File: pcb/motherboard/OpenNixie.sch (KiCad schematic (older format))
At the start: 137 parts, among them J1 Conn_01x02, J10 Conn_01x10, J2 Conn_01x03, J3 Conn_01x03, J4 DC 12V, J5 Conn_01x04, J6 Conn_01x03, J7 Conn_01x10, J8 Conn_01x10, J9 Conn_01x10, Q1 S8050, Q10 MPSA42, Q11 MPSA42, Q12 MPSA42, Q13 MPSA42, Q14 MPSA42, Q15 MPSA42, Q16 MPSA42, Q17 MPSA42, Q18 MPSA42, Q19 MPSA42, Q2 IRFB4620, Q20 MPSA42, Q21 MPSA42, Q22 MPSA42, Q23 MPSA42, Q24 MPSA42, Q25 MPSA42, Q26 MPSA42, Q27 MPSA42, Q28 MPSA42, Q29 MPSA42, Q3 MPSA42, Q30 MPSA42, Q31 MPSA42, Q32 MPSA42, Q33 MPSA42, Q34 MPSA42, Q35 MPSA42, Q36 MPSA42, Q37 MPSA42, Q38 MPSA42, Q39 MPSA42, Q4 MPSA42, Q40 MPSA42, Q41 MPSA42, Q42 MPSA42, Q5 MPSA42, Q6 MPSA42, Q7 MPSA42, Q8 MPSA42, Q9 MPSA42, SW1 SW_SPST, U1 LM7805_TO220, U10 74LS138, U11 74LS138, U12 74LS138, U13 74LS138, U14 74HC595, U15 74LS138, U16 74LS138, U2 NE555P, U3 MAX1771CSA, U4 DS3231M, U5 24LC16, U6 TSDP341xx, U7 74LS138, U8 74LS138, U9 74HC595

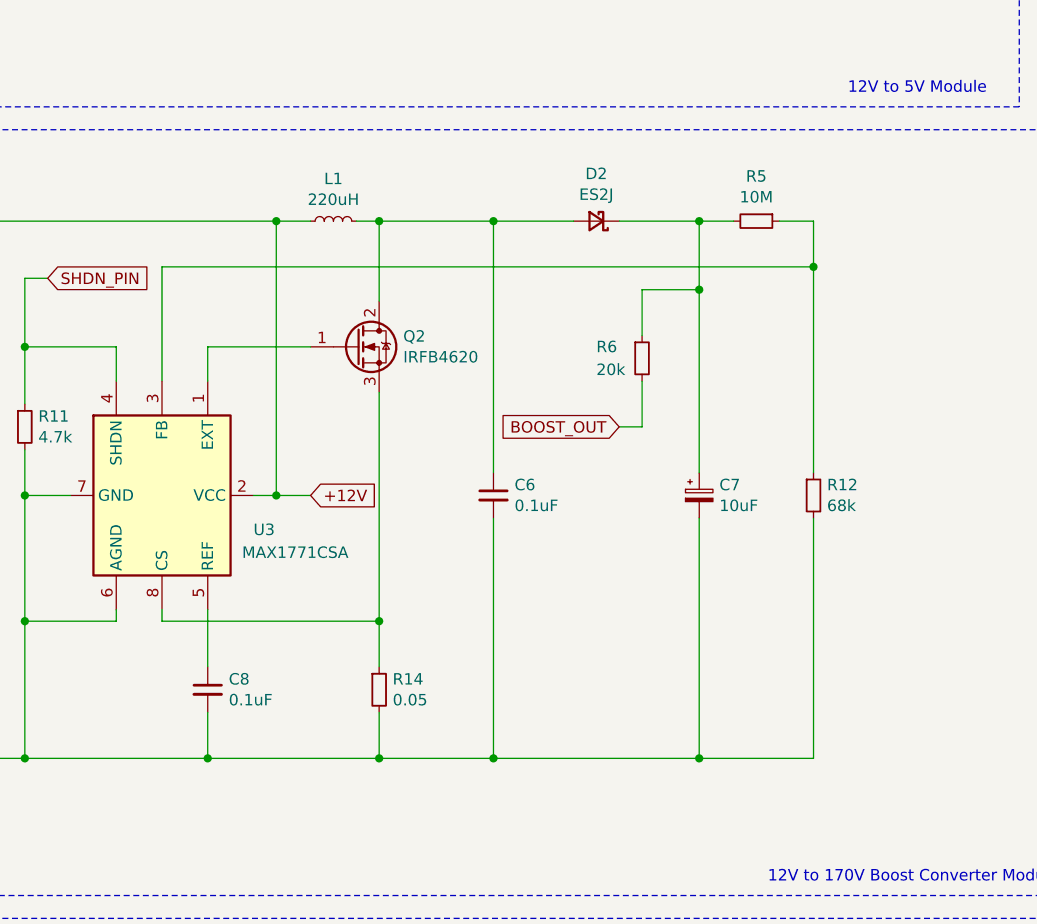
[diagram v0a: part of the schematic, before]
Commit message: Fix layout errors
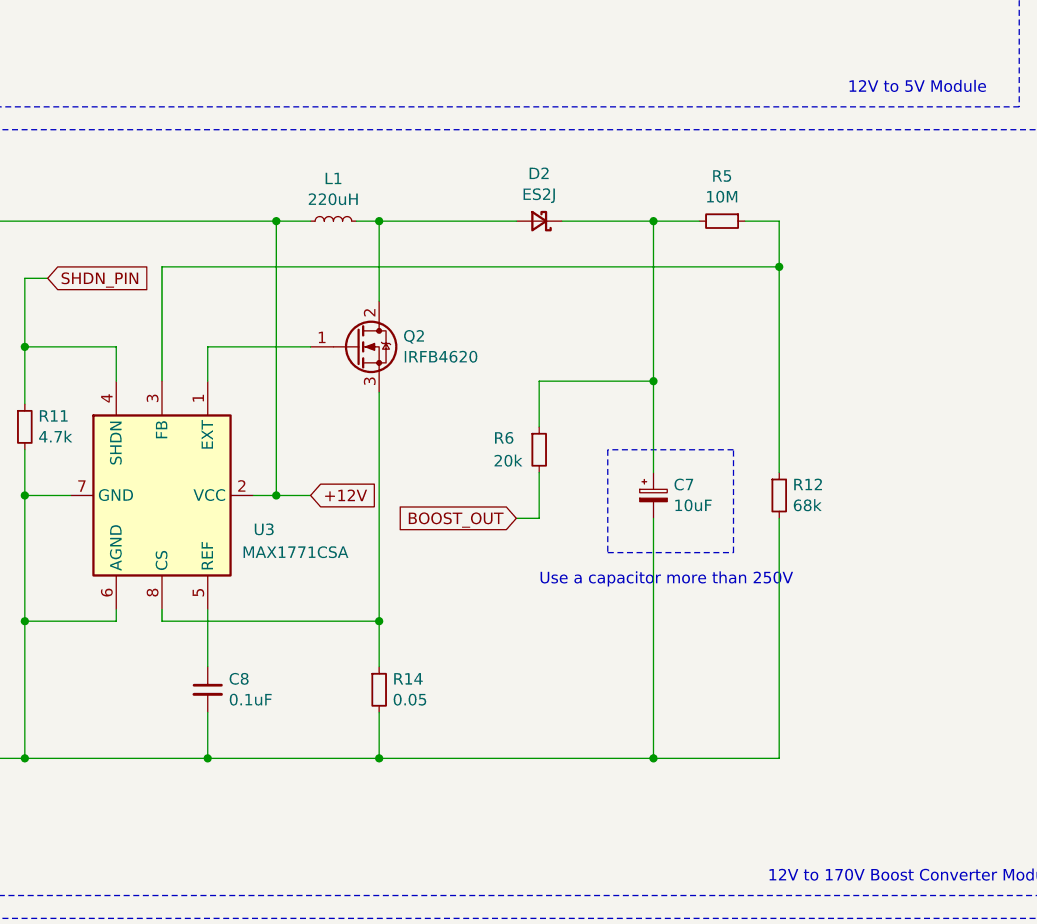
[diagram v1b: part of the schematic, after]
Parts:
- removed C6: 0.1uF, Capacitor_THT:C_Disc_D3.0mm_W2.0mm_P2.50mm, symbol Device:C_Small
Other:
- note added: "Use a capacitor more than 250V"
- moved on the sheet: C7, D2, R12, R5, R6
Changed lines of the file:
@@
 Connection ~ 9500 2450
 Wire Wire Line
-	4950 6100 5450 6100
-Connection ~ 4950 6100
+	4250 4450 4750 4450
 Wire Wire Line
-	4700 4050 4950 4050
-Wire Wire Line
-	2600 3950 5450 3950
-Wire Wire Line
-	4050 6100 4950 6100
-Text GLabel 4600 4650 0    50   Input ~ 0
+	2600 3950 5300 3950
+Text GLabel 4150 5050 0    50   Input ~ 0
 BOOST_OUT
 Wire Wire Line
@@
 Text GLabel 2100 4000 2    50   Input ~ 0
 SHDN_PIN
-Connection ~ 5450 3950
+Connection ~ 5300 3950
 Wire Wire Line
-	5450 3950 5450 4850
+	5300 3950 5300 4850
 Connection ~ 3100 4950
 Wire Wire Line
@@
 	2600 5450 2600 5500
 Wire Wire Line
-	3550 6100 4050 6100
-Connection ~ 4050 6100
-Wire Wire Line
-	4950 5050 4950 6100
+	4750 5050 4750 6100
 $Comp
 L Device:CP_Small C7
 U 1 1 63E82EE3
-P 4950 4950
-F 0 "C7" H 5038 4996 50  0000 L CNN
-F 1 "10uF" H 5038 4905 50  0000 L CNN
-F 2 "Capacitor_THT:CP_Radial_D5.0mm_P2.50mm" H 4950 4950 50  0001 C CNN
-F 3 "~" H 4950 4950 50  0001 C CNN
-	1    4950 4950
+P 4750 4950
+F 0 "C7" H 4838 4996 50  0000 L CNN
+F 1 "10uF" H 4838 4905 50  0000 L CNN
+F 2 "Capacitor_THT:CP_Radial_D5.0mm_P2.50mm" H 4750 4950 50  0001 C CNN
+F 3 "~" H 4750 4950 50  0001 C CNN
+	1    4750 4950
 	1    0    0    -1
 $EndComp
 Wire Wire Line
-	5450 5050 5450 6100
+	5300 5050 5300 6100
 $Comp
 L Device:R_Small R12
 U 1 1 63E66239
-P 5450 4950
-F 0 "R12" H 5509 4996 50  0000 L CNN
-F 1 "68k" H 5509 4905 50  0000 L CNN
-F 2 "Resistor_THT:R_Axial_DIN0204_L3.6mm_D1.6mm_P7.62mm_Horizontal" H 5450 4950 50  0001 C CNN
-F 3 "~" H 5450 4950 50  0001 C CNN
-	1    5450 4950
+P 5300 4950
+F 0 "R12" H 5359 4996 50  0000 L CNN
+F 1 "68k" H 5359 4905 50  0000 L CNN
+F 2 "Resistor_THT:R_Axial_DIN0204_L3.6mm_D1.6mm_P7.62mm_Horizontal" H 5300 4950 50  0001 C CNN
+F 3 "~" H 5300 4950 50  0001 C CNN
+	1    5300 4950
 	1    0    0    -1
 $EndComp
@@
 	1    0    0    -1
 $EndComp
-Wire Wire Line
-	4050 5050 4050 6100
-$Comp
-L Device:C_Small C6
-U 1 1 63DAEE6F
-P 4050 4950
-F 0 "C6" H 4142 4996 50  0000 L CNN
-F 1 "0.1uF" H 4142 4905 50  0000 L CNN
-F 2 "Capacitor_THT:C_Disc_D3.0mm_W2.0mm_P2.50mm" H 4050 4950 50  0001 C CNN
-F 3 "~" H 4050 4950 50  0001 C CNN
-	1    4050 4950
-	1    0    0    -1
-$EndComp
 Connection ~ 2800 6100
 Wire Wire Line
@@
 $EndComp
 Wire Wire Line
-	4600 4650 4700 4650
-Connection ~ 4950 4050
-Wire Wire Line
-	4950 4050 4950 4850
+	4150 5050 4250 5050
 Wire Wire Line
-	4700 4050 4700 4250
+	4250 4450 4250 4650
 Wire Wire Line
-	4700 4450 4700 4650
+	4250 4850 4250 5050
 $Comp
 L Device:R_Small R6
 U 1 1 6A87AE72
-P 4700 4350
-F 0 "R6" H 4500 4400 50  0000 L CNN
-F 1 "20k" H 4500 4300 50  0000 L CNN
-F 2 "Resistor_THT:R_Axial_DIN0204_L3.6mm_D1.6mm_P7.62mm_Horizontal" H 4700 4350 50  0001 C CNN
-F 3 "~" H 4700 4350 50  0001 C CNN
-	1    4700 4350
+P 4250 4750
+F 0 "R6" H 4050 4800 50  0000 L CNN
+F 1 "20k" H 4050 4700 50  0000 L CNN
+F 2 "Resistor_THT:R_Axial_DIN0204_L3.6mm_D1.6mm_P7.62mm_Horizontal" H 4250 4750 50  0001 C CNN
+F 3 "~" H 4250 4750 50  0001 C CNN
+	1    4250 4750
 	1    0    0    -1
 $EndComp
@@
 	1    0    0    -1
 $EndComp
-Wire Wire Line
-	4950 4050 4950 3750
 $Comp
 L Device:L_Small L1
@@
 $EndComp
 Wire Wire Line
-	4050 3750 4050 4850
-Wire Wire Line
 	1500 4850 1500 3750
 $Comp
 L Device:D_Schottky_Small D2
 U 1 1 63E25C25
-P 4500 3750
-F 0 "D2" H 4500 3543 50  0000 C CNN
-F 1 "ES2J" H 4500 3634 50  0000 C CNN
-F 2 "Diode_SMD:D_SMA" V 4500 3750 50  0001 C CNN
-F 3 "~" V 4500 3750 50  0001 C CNN
-	1    4500 3750
+P 4250 3750
+F 0 "D2" H 4250 3543 50  0000 C CNN
+F 1 "ES2J" H 4250 3634 50  0000 C CNN
+F 2 "Diode_SMD:D_SMA" V 4250 3750 50  0001 C CNN
+F 3 "~" V 4250 3750 50  0001 C CNN
+	1    4250 3750
 	-1   0    0    1
 $EndComp
 Wire Wire Line
-	4600 3750 4950 3750
+	4350 3750 4750 3750
 $Comp
 L Device:R_Small R5
 U 1 1 63E5A426
-P 5200 3750
-F 0 "R5" V 5004 3750 50  0000 C CNN
-F 1 "10M" V 5095 3750 50  0000 C CNN
-F 2 "Resistor_THT:R_Axial_DIN0204_L3.6mm_D1.6mm_P7.62mm_Horizontal" H 5200 3750 50  0001 C CNN
-F 3 "~" H 5200 3750 50  0001 C CNN
-	1    5200 3750
+P 5050 3750
+F 0 "R5" V 4854 3750 50  0000 C CNN
+F 1 "10M" V 4945 3750 50  0000 C CNN
+F 2 "Resistor_THT:R_Axial_DIN0204_L3.6mm_D1.6mm_P7.62mm_Horizontal" H 5050 3750 50  0001 C CNN
+F 3 "~" H 5050 3750 50  0001 C CNN
+	1    5050 3750
 	0    1    1    0
 $EndComp
 Wire Wire Line
-	5300 3750 5450 3750
-Connection ~ 4050 3750
-Wire Wire Line
-	4050 3750 4400 3750
+	5150 3750 5300 3750
 Wire Wire Line
 	1500 3750 3100 3750
@@
 	3100 3750 3100 4950
 Wire Wire Line
-	3550 3750 4050 3750
-Wire Wire Line
 	3450 3750 3550 3750
 Connection ~ 3550 3750
@@
 	3550 3750 3550 4100
 Wire Wire Line
-	5450 3750 5450 3950
-Connection ~ 4950 3750
-Wire Wire Line
-	4950 3750 5100 3750
+	5300 3750 5300 3950
 Wire Notes Line
 	15300 3250 22800 3250
@@
 	1    0    0    -1
 $EndComp
+Wire Wire Line
+	3550 6100 4750 6100
+Wire Wire Line
+	3550 3750 4150 3750
+Connection ~ 4750 4450
+Wire Wire Line
+	4750 4450 4750 4850
+Wire Wire Line
+	4750 3750 4750 4450
+Connection ~ 4750 3750
+Connection ~ 4750 6100
+Wire Wire Line
+	4750 6100 5300 6100
+Wire Wire Line
+	4750 3750 4950 3750
+Wire Notes Line
+	4550 4750 4550 5200
+Wire Notes Line
+	4550 5200 5100 5200
+Wire Notes Line
+	5100 5200 5100 4750
+Wire Notes Line
+	5100 4750 4550 4750
+Text Notes 4250 5350 0    50   ~ 0
+Use a capacitor more than 250V
 Wire Bus Line
 	11050 13150 11050 14500

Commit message: Change footprint
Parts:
- C7: footprint Capacitor_THT:CP_Radial_D5.0mm_P2.50mm -> Capacitor_THT:CP_Radial_D8.0mm_P3.80mm
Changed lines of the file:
@@
 F 0 "C7" H 4838 4996 50  0000 L CNN
 F 1 "10uF" H 4838 4905 50  0000 L CNN
-F 2 "Capacitor_THT:CP_Radial_D5.0mm_P2.50mm" H 4750 4950 50  0001 C CNN
+F 2 "Capacitor_THT:CP_Radial_D8.0mm_P3.80mm" H 4750 4950 50  0001 C CNN
 F 3 "~" H 4750 4950 50  0001 C CNN
 	1    4750 4950

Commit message: Fixes
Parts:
- removed Q2: IRFB4620, Package_TO_SOT_THT:TO-220-3_Horizontal_TabDown, symbol Nixie_Clock:IRFB4620
- added Q2: TK8P65W, Package_TO_SOT_SMD:TO-252-2, symbol Nixie_Clock:TK8P65W
- R6: value 20k -> 47k
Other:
- moved on the sheet: D2
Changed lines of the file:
@@
 Wire Wire Line
 	5300 5050 5300 6100
-$Comp
-L Device:R_Small R12
-U 1 1 63E66239
-P 5300 4950
-F 0 "R12" H 5359 4996 50  0000 L CNN
-F 1 "68k" H 5359 4905 50  0000 L CNN
-F 2 "Resistor_THT:R_Axial_DIN0204_L3.6mm_D1.6mm_P7.62mm_Horizontal" H 5300 4950 50  0001 C CNN
-F 3 "~" H 5300 4950 50  0001 C CNN
-	1    5300 4950
-	1    0    0    -1
-$EndComp
 Wire Wire Line
 	2000 4300 2400 4300
@@
 	4250 4850 4250 5050
 $Comp
-L Device:R_Small R6
-U 1 1 6A87AE72
-P 4250 4750
-F 0 "R6" H 4050 4800 50  0000 L CNN
-F 1 "20k" H 4050 4700 50  0000 L CNN
-F 2 "Resistor_THT:R_Axial_DIN0204_L3.6mm_D1.6mm_P7.62mm_Horizontal" H 4250 4750 50  0001 C CNN
-F 3 "~" H 4250 4750 50  0001 C CNN
-	1    4250 4750
-	1    0    0    -1
-$EndComp
-$Comp
 L Nixie_Clock:MAX1771CSA U3
 U 1 1 63E16B68
@@
 	2800 4300 3250 4300
 $Comp
-L Nixie_Clock:IRFB4620 Q2
-U 1 1 63FF12BB
-P 3450 4300
-F 0 "Q2" H 3655 4346 50  0000 L CNN
-F 1 "IRFB4620" H 3655 4255 50  0000 L CNN
-F 2 "Package_TO_SOT_THT:TO-220-3_Horizontal_TabDown" H 3450 4300 50  0001 C CIN
-F 3 "" H 3450 4300 50  0001 L CNN
-	1    3450 4300
-	1    0    0    -1
-$EndComp
-$Comp
 L Device:L_Small L1
 U 1 1 63D8F31B
@@
 L Device:D_Schottky_Small D2
 U 1 1 63E25C25
-P 4250 3750
-F 0 "D2" H 4250 3543 50  0000 C CNN
-F 1 "ES2J" H 4250 3634 50  0000 C CNN
-F 2 "Diode_SMD:D_SMA" V 4250 3750 50  0001 C CNN
-F 3 "~" V 4250 3750 50  0001 C CNN
-	1    4250 3750
+P 4150 3750
+F 0 "D2" H 4150 3543 50  0000 C CNN
+F 1 "ES2J" H 4150 3634 50  0000 C CNN
+F 2 "Diode_SMD:D_SMA" V 4150 3750 50  0001 C CNN
+F 3 "~" V 4150 3750 50  0001 C CNN
+	1    4150 3750
 	-1   0    0    1
 $EndComp
 Wire Wire Line
-	4350 3750 4750 3750
-$Comp
-L Device:R_Small R5
-U 1 1 63E5A426
-P 5050 3750
-F 0 "R5" V 4854 3750 50  0000 C CNN
-F 1 "10M" V 4945 3750 50  0000 C CNN
-F 2 "Resistor_THT:R_Axial_DIN0204_L3.6mm_D1.6mm_P7.62mm_Horizontal" H 5050 3750 50  0001 C CNN
-F 3 "~" H 5050 3750 50  0001 C CNN
-	1    5050 3750
-	0    1    1    0
-$EndComp
+	4250 3750 4750 3750
 Wire Wire Line
 	5150 3750 5300 3750
@@
 	3550 6100 4750 6100
 Wire Wire Line
-	3550 3750 4150 3750
+	3550 3750 4050 3750
 Connection ~ 4750 4450
 Wire Wire Line
@@
 Wire Notes Line
 	5100 4750 4550 4750
+$Comp
+L Nixie_Clock:TK8P65W Q2
+U 1 1 641075BE
+P 3450 4300
+F 0 "Q2" H 3654 4346 50  0000 L CNN
+F 1 "TK8P65W" H 3654 4255 50  0000 L CNN
+F 2 "Package_TO_SOT_SMD:TO-252-2" H 3450 4300 50  0001 C CIN
+F 3 "" H 3450 4300 50  0001 L CNN
+	1    3450 4300
+	1    0    0    -1
+$EndComp
+$Comp
+L Device:R_Small R12
+U 1 1 63E66239
+P 5300 4950
+F 0 "R12" H 5359 4996 50  0000 L CNN
+F 1 "68k" H 5359 4905 50  0000 L CNN
+F 2 "Resistor_THT:R_Axial_DIN0204_L3.6mm_D1.6mm_P7.62mm_Horizontal" H 5300 4950 50  0001 C CNN
+F 3 "~" H 5300 4950 50  0001 C CNN
+	1    5300 4950
+	1    0    0    -1
+$EndComp
+$Comp
+L Device:R_Small R5
+U 1 1 63E5A426
+P 5050 3750
+F 0 "R5" V 4854 3750 50  0000 C CNN
+F 1 "10M" V 4945 3750 50  0000 C CNN
+F 2 "Resistor_THT:R_Axial_DIN0204_L3.6mm_D1.6mm_P7.62mm_Horizontal" H 5050 3750 50  0001 C CNN
+F 3 "~" H 5050 3750 50  0001 C CNN
+	1    5050 3750
+	0    1    1    0
+$EndComp
 Text Notes 4250 5350 0    50   ~ 0
 Use a capacitor more than 250V
+$Comp
+L Device:R_Small R6
+U 1 1 6A87AE72
+P 4250 4750
+F 0 "R6" H 4050 4800 50  0000 L CNN
+F 1 "47k" H 4050 4700 50  0000 L CNN
+F 2 "Resistor_THT:R_Axial_DIN0204_L3.6mm_D1.6mm_P7.62mm_Horizontal" H 4250 4750 50  0001 C CNN
+F 3 "~" H 4250 4750 50  0001 C CNN
+	1    4250 4750
+	1    0    0    -1
+$EndComp
 Wire Bus Line
 	11050 13150 11050 14500

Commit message: Updates on resistor values
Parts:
- R6: value 47k -> 20k
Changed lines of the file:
@@
 P 4250 4750
 F 0 "R6" H 4050 4800 50  0000 L CNN
-F 1 "47k" H 4050 4700 50  0000 L CNN
+F 1 "20k" H 4050 4700 50  0000 L CNN
 F 2 "Resistor_THT:R_Axial_DIN0204_L3.6mm_D1.6mm_P7.62mm_Horizontal" H 4250 4750 50  0001 C CNN
 F 3 "~" H 4250 4750 50  0001 C CNN
